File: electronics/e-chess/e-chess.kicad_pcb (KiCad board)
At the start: 2 copper layers, 4 parts, among them J1 WS2812_LEDs, U1 MCP23017_SP, U2 ESP32-S3

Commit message: Draw PCB
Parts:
- removed D2: 1N4001, Diode_THT:D_DO-41_SOD81_P10.16mm_Horizontal
- removed U2: ESP32-S3, PCM_Espressif:ESP32-S3-DevKitC
- added C2: 470 µF, Capacitor_THT:CP_Radial_D10.0mm_P5.00mm, F.Cu at (255.5, 96.4)
- added J2: Outputs, TerminalBlock_Phoenix:TerminalBlock_Phoenix_MKDS-1,5-8-5.08_1x08_P5.08mm_Horizontal, F.Cu at (174.6, 109.0)
- added J3: Inputs, TerminalBlock_Phoenix:TerminalBlock_Phoenix_MKDS-1,5-8-5.08_1x08_P5.08mm_Horizontal, F.Cu at (210.3, 80.0)
- added J4: e-Paper 1.54 inch, TerminalBlock_Phoenix:TerminalBlock_Phoenix_MKDS-1,5-8-5.08_1x08_P5.08mm_Horizontal, F.Cu at (252.4, 80.0)
- added J5: Arbitary I/O, TerminalBlock_Phoenix:TerminalBlock_Phoenix_MKDS-1,5-8-5.08_1x08_P5.08mm_Horizontal, F.Cu at (216.7, 109.0)
- added J6: Power for I/O, TerminalBlock_Phoenix:TerminalBlock_Phoenix_MKDS-1,5-4-5.08_1x04_P5.08mm_Horizontal, F.Cu at (266.7, 111.2)
- added R1: R4.7k, Resistor_THT:R_Axial_DIN0207_L6.3mm_D2.5mm_P7.62mm_Horizontal, F.Cu at (169.7, 99.0)
- added R2: R4.7k, Resistor_THT:R_Axial_DIN0207_L6.3mm_D2.5mm_P7.62mm_Horizontal, F.Cu at (166.0, 99.0)
- added R3: R470, Resistor_THT:R_Axial_DIN0207_L6.3mm_D2.5mm_P7.62mm_Horizontal, F.Cu at (258.2, 84.1)
- added REF00: MountingHole_4mm, MountingHole:MountingHole_4mm, F.Cu at (97.1, 78.8)
- added REF01: MountingHole_4mm, MountingHole:MountingHole_4mm, F.Cu at (97.1, 110.2)
- added REF02: MountingHole_4mm, MountingHole:MountingHole_4mm, F.Cu at (241.5, 94.0)
- added U3: ESP32-S3-DevKitC, PCM_Espressif:ESP32-S3-DevKitC, F.Cu at (155.9, 83.0)
- moved J1 134.8 mm to (266.7, 88.1), turned to 90 degrees
- moved U1 78.9 mm to (174.7, 99.1), turned to 90 degrees
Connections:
- J1 pad 2: unconnected-(J1-DIN-Pad2) -> Net-(J1-DIN)
- U1 pad 2: unconnected-(U1-GPB1-Pad2) -> Net-(J2-Pin_2)
- U1 pad 21: unconnected-(U1-GPA0-Pad21) -> Net-(J3-Pin_1)
- U1 pad 22: unconnected-(U1-GPA1-Pad22) -> Net-(J3-Pin_2)
- U1 pad 23: unconnected-(U1-GPA2-Pad23) -> Net-(J3-Pin_3)
- U1 pad 24: unconnected-(U1-GPA3-Pad24) -> Net-(J3-Pin_4)
- U1 pad 25: unconnected-(U1-GPA4-Pad25) -> Net-(J3-Pin_5)
- U1 pad 26: unconnected-(U1-GPA5-Pad26) -> Net-(J3-Pin_6)
- U1 pad 27: unconnected-(U1-GPA6-Pad27) -> Net-(J3-Pin_7)
- U1 pad 3: unconnected-(U1-GPB2-Pad3) -> Net-(J2-Pin_3)
- U1 pad 4: unconnected-(U1-GPB3-Pad4) -> Net-(J2-Pin_4)
- U1 pad 5: unconnected-(U1-GPB4-Pad5) -> Net-(J2-Pin_5)
- U1 pad 6: unconnected-(U1-GPB5-Pad6) -> Net-(J2-Pin_6)
- U1 pad 7: unconnected-(U1-GPB6-Pad7) -> Net-(J2-Pin_7)
- U1 pad 8: unconnected-(U1-GPB7-Pad8) -> Net-(J2-Pin_8)
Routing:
- net +5V: track 0.00 -> 197.3 mm
- net +3.3V: track 0.00 -> 164.6 mm
- net Net-(J5-GPIO46): track 0.00 -> 145.6 mm, vias 0 -> 1
- net Net-(J5-GPIO48): track 0.00 -> 140.4 mm, vias 0 -> 1
- net Net-(J4-DIN): track 0.00 -> 139.2 mm
- net Net-(J5-GPIO47): track 0.00 -> 136.8 mm
- net Net-(J4-CLK): track 0.00 -> 131.2 mm
- net Net-(J5-GPIO45): track 0.00 -> 120.8 mm
- net Net-(U3-GPIO4/ADC1_CH3): track 0.00 -> 112.3 mm
- net Net-(J4-CS): track 0.00 -> 110.9 mm, vias 0 -> 1
- net Net-(J4-RST): track 0.00 -> 110.6 mm
- net Net-(J4-DC): track 0.00 -> 103.9 mm
- net Net-(J5-GPIO38): track 0.00 -> 101.5 mm
- net Net-(J5-GPIO37): track 0.00 -> 99.2 mm
- net Net-(J5-GPIO36): track 0.00 -> 98.8 mm, vias 0 -> 1
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- added copper zone on B.Cu, net GND
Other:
- board outline added: 179.4 x 40 mm
- board text added: "github.com/aligator/e-chess"

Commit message: change exposed pins a bit
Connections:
- J5 pad 5: Net-(J5-GPIO45) -> Net-(J5-GPIO21)
- J5 pad 6: Net-(J5-GPIO46) -> Net-(J5-GPIO18)
- U3 pad 11: unconnected-(U3-GPIO18/ADC2_CH7-Pad11) -> Net-(J5-GPIO18)
- U3 pad 14: Net-(J5-GPIO46) -> unconnected-(U3-GPIO46-Pad14)
- U3 pad 27: unconnected-(U3-GPIO21-Pad27) -> Net-(J5-GPIO21)
- U3 pad 30: Net-(J5-GPIO45) -> unconnected-(U3-GPIO45-Pad30)
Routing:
- net Net-(J5-GPIO46): track 145.6 -> 0.00 mm, vias 1 -> 0
- net Net-(J5-GPIO18): track 0.00 -> 133.0 mm, vias 0 -> 1
- net Net-(J5-GPIO21): track 0.00 -> 128.4 mm
- net Net-(J5-GPIO45): track 120.8 -> 0.00 mm
- net +3.3V: track 164.6 -> 148.9 mm, vias 0 -> 1
- net Net-(J2-Pin_5): track 14.2 -> 19.8 mm
- net Net-(J2-Pin_4): track 13.0 -> 16.4 mm
- net Net-(J4-DC): track 103.9 -> 106.9 mm, vias 0 -> 1
- net Net-(J5-GPIO36): track 98.8 -> 95.9 mm, vias 1 -> 0
- net +5V: track 197.3 -> 194.5 mm, vias 0 -> 1
- net Net-(J4-DIN): track 139.2 -> 140.7 mm, vias 0 -> 1
- net Net-(J4-BUSY): track 75.9 -> 74.6 mm, vias 1 -> 0
- net Net-(U1-SCK): track 96.7 -> 98.1 mm
- net Net-(J5-GPIO38): track 101.5 -> 102.7 mm
- net Net-(J5-GPIO47): track 136.8 -> 135.7 mm
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
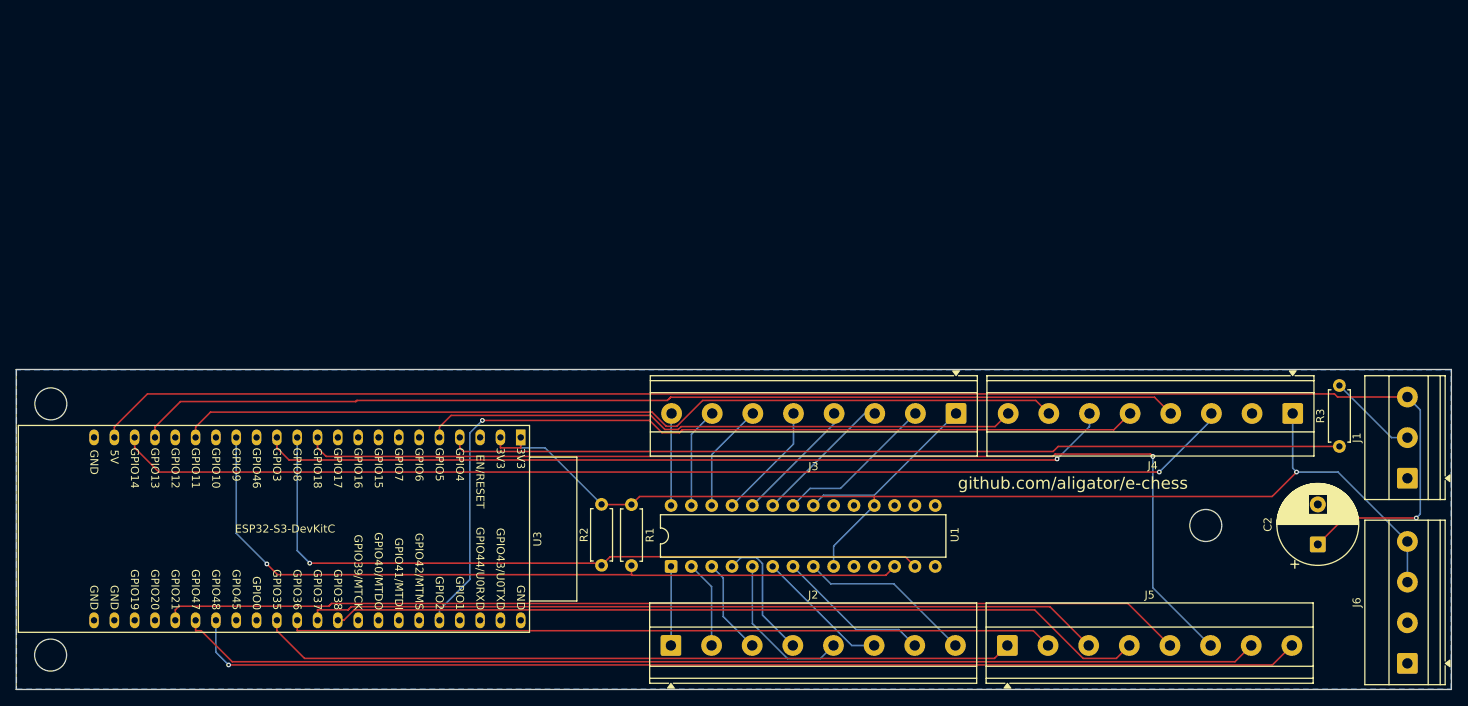
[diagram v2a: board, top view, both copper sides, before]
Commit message: Move terminals a bit in to have more space for the cables
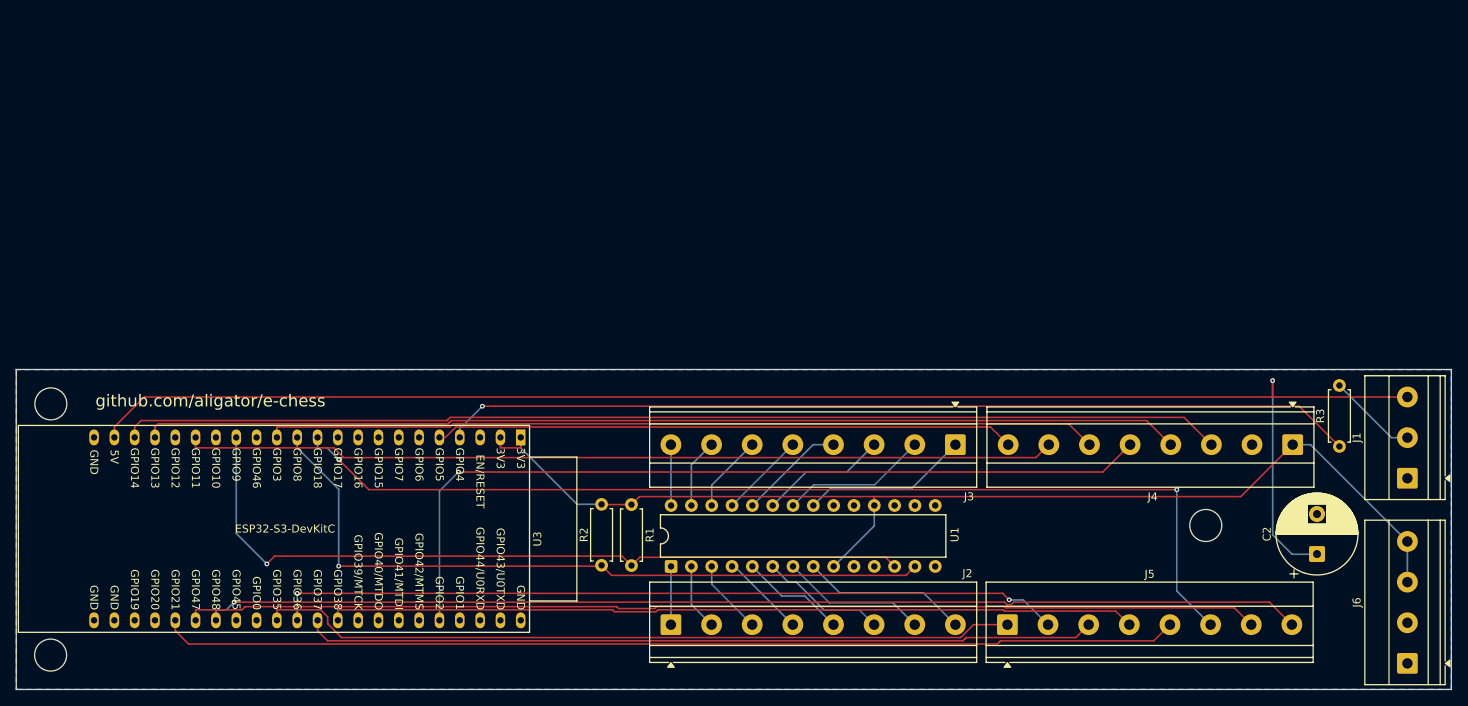
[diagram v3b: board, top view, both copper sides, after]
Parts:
- moved J3 3.90 mm to (210.2, 83.9)
- moved J4 3.90 mm to (252.4, 83.9)
- moved J2 2.60 mm to (174.6, 106.4)
- moved J5 2.60 mm to (216.7, 106.4)
- moved C2 1.20 mm to (255.4, 97.6)
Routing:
- net Net-(J2-Pin_5): track 19.8 -> 13.2 mm
- net Net-(J2-Pin_4): track 16.4 -> 10.6 mm
- net Net-(J4-CS): track 110.0 -> 104.9 mm
- net +3.3V: track 148.9 -> 144.2 mm, vias 1 -> 0
- net Net-(J3-Pin_7): track 12.6 -> 8.64 mm
- net Net-(J3-Pin_5): track 14.7 -> 10.7 mm
- net Net-(J3-Pin_6): track 13.6 -> 9.70 mm
- net Net-(J3-Pin_8): track 11.5 -> 7.61 mm
- net Net-(J5-GPIO18): track 133.0 -> 129.5 mm, vias 1 -> 2
- net Net-(J5-GPIO36): track 95.9 -> 98.8 mm, vias 0 -> 2
- net Net-(U3-GPIO4/ADC1_CH3): track 111.7 -> 114.4 mm, vias 0 -> 1
- net Net-(J4-DIN): track 140.7 -> 138.0 mm, vias 1 -> 0
- net Net-(J2-Pin_1): track 9.89 -> 7.29 mm
- net Net-(J2-Pin_3): track 12.0 -> 9.38 mm
- net Net-(J2-Pin_2): track 10.9 -> 8.32 mm
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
